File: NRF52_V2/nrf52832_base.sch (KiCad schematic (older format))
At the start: 22 parts

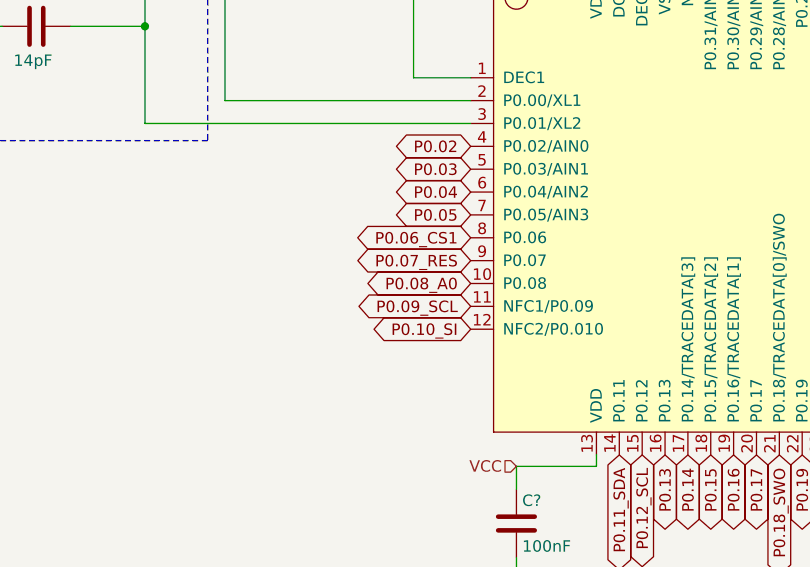
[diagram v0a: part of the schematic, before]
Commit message: Added GPIO pin headers, buttons, and LEDs.
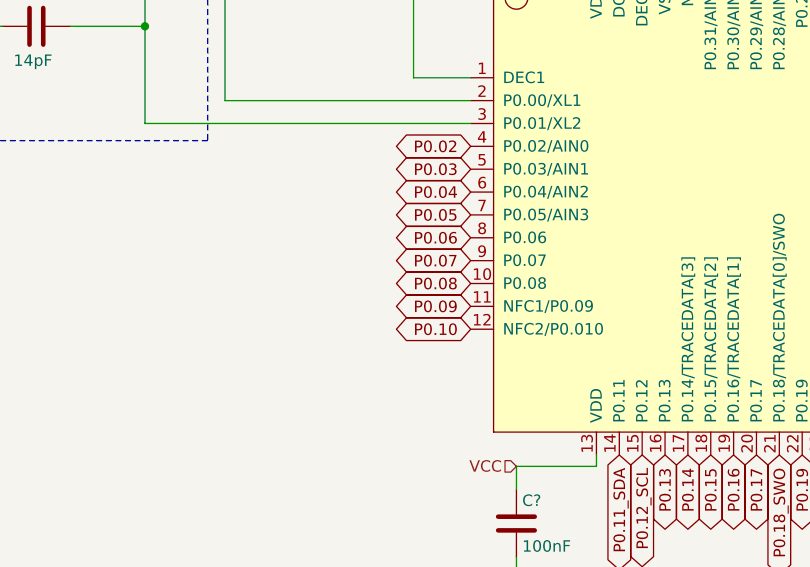
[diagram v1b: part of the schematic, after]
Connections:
- net P0.06_CS1 renamed P0.06
- net P0.07_RES renamed P0.07
- net P0.08_A0 renamed P0.08
- net P0.09_SCL renamed P0.09
- net P0.10_SI renamed P0.10
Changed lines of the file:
@@
 P0.05
 Text GLabel 4150 4050 0    50   BiDi ~ 0
-P0.06_CS1
+P0.06
 Text GLabel 4150 4150 0    50   BiDi ~ 0
-P0.07_RES
+P0.07
 Text GLabel 4150 4250 0    50   BiDi ~ 0
-P0.08_A0
+P0.08
 Text GLabel 4150 4350 0    50   BiDi ~ 0
-P0.09_SCL
+P0.09
 Text GLabel 4150 4450 0    50   BiDi ~ 0
-P0.10_SI
+P0.10
 Text GLabel 6350 4050 2    50   BiDi ~ 0
 P0.24
